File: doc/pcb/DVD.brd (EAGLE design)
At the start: 53.7 x 42.8 mm, 34 parts, among them IC1 7805, IC2 74HC14N

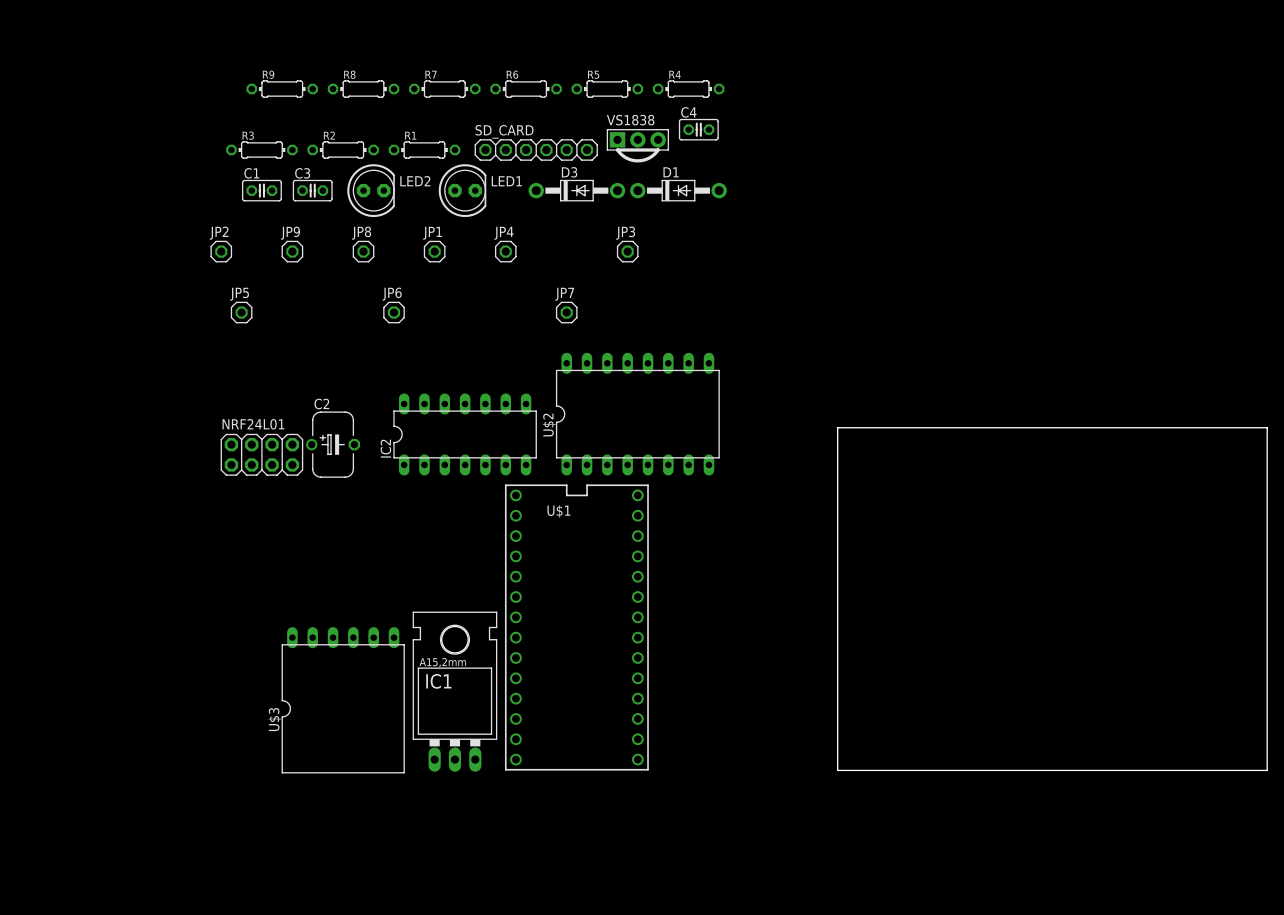
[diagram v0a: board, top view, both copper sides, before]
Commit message: PCB moved/added capacitors, changed voltage Pololu/BNO055, added pinouts & testpoints
Only 1 testpoint connected
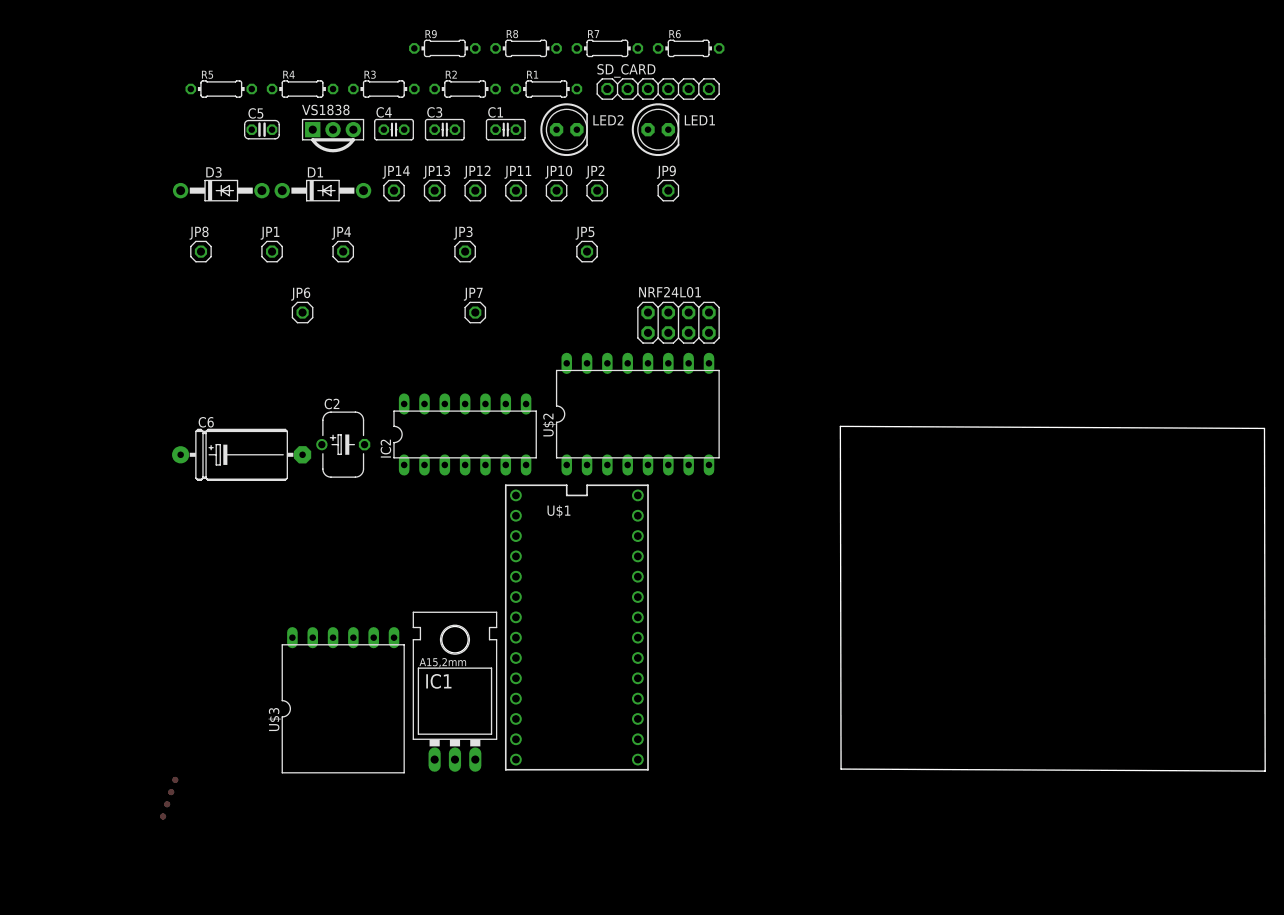
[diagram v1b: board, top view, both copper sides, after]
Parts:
- added C5: 100nF, rcl:C025-024X044
- added C6: 100uF, resistor:E15-6
- added JP10: P2, pinhead:1X01
- added JP11: P5, pinhead:1X01
- added JP12: P6, pinhead:1X01
- added JP13: P7, pinhead:1X01
- added JP14: P17, pinhead:1X01
- added TP1, TP2, TP3, TP4: TEST-POINT3, SparkFun-Passives:PAD.03X.03
- C1: value 0.1 uF -> 100 nF
- C2: value 1000 uF -> 0.22F
- R2, R4: value 3.3K -> 5.6K
- moved NRF24L01 54.6 mm to (-19.1, 57.1)
- moved R4 48.3 mm to (-66.0, 86.4)
- moved R5 48.3 mm to (-76.2, 86.4)
- moved JP2 47.6 mm to (-29.2, 73.7)
- moved JP9 47.6 mm to (-20.3, 73.7)
- moved D1 44.5 mm to (-63.5, 73.7)
- moved D3 44.5 mm to (-76.2, 73.7)
- moved JP5 43.8 mm to (-30.5, 66.0)
- moved VS1838 38.1 mm to (-62.2, 81.3)
- moved C4 38.1 mm to (-54.6, 81.3)
- moved C1 31.4 mm to (-40.6, 81.3)
- moved LED1 25.3 mm to (-21.6, 81.3)
- moved LED2 25.3 mm to (-33.0, 81.3)
- moved R6 20.9 mm to (-17.8, 91.4)
- moved R8 20.9 mm to (-38.1, 91.4)
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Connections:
- removed net N$8: LED2.A, R9.1
- new net N$4: LED2.K, R9.2
- net +3V3: no longer U$2.2, U$3.1
- net +5V: now also C1.1, C5.1, LED2.A, TP1.P$1, U$2.2, U$3.1; no longer SD_CARD.5
- net GND: now also C5.2, C6.-; no longer LED2.K
- net N$19: now also R9.1; no longer R9.2
- net N$20: now also JP10.1
- net N$21: now also JP12.1
- net N$22: now also JP13.1
- net N$3: now also JP11.1
- net N$6: now also JP14.1
- net V+: now also C6.+; no longer C1.1
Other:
- board size 53.7 x 42.8 mm -> 53.1 x 43.1 mm

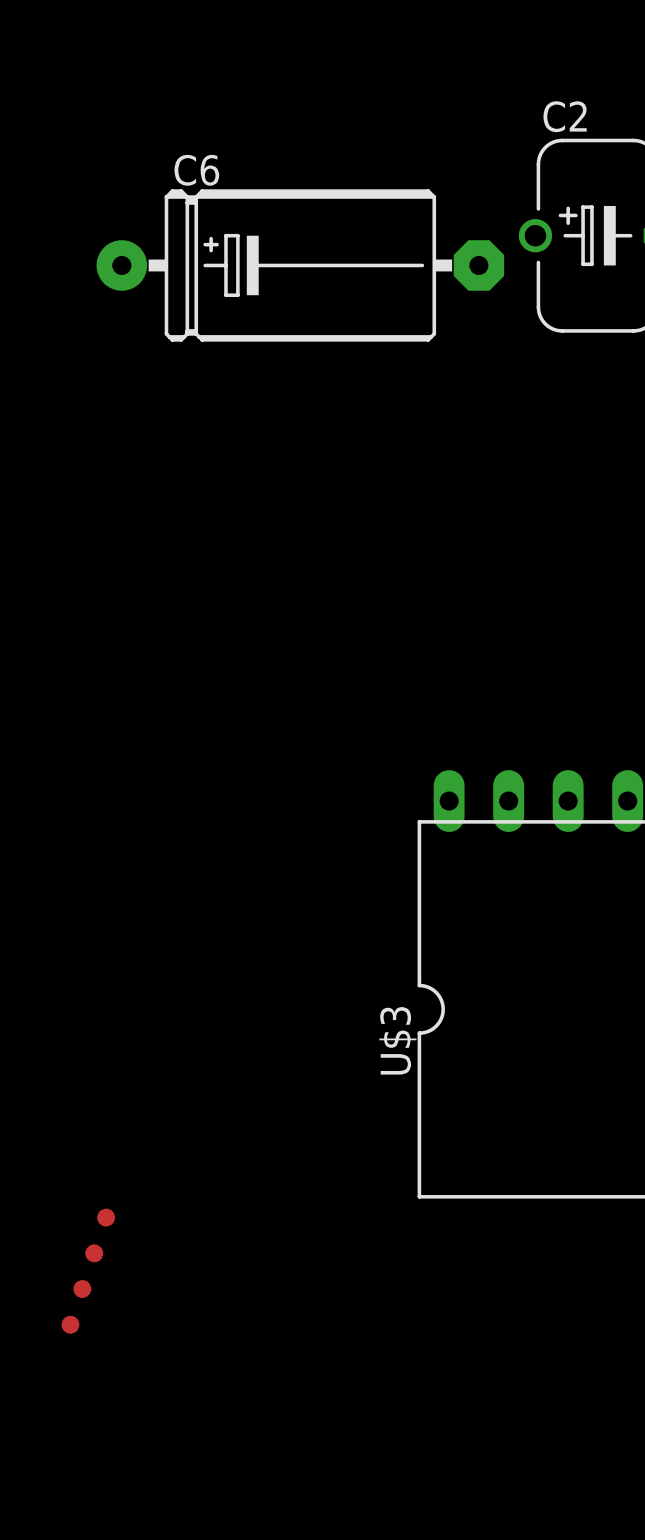
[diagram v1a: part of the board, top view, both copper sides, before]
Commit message: Replaced axial by radial capacitor
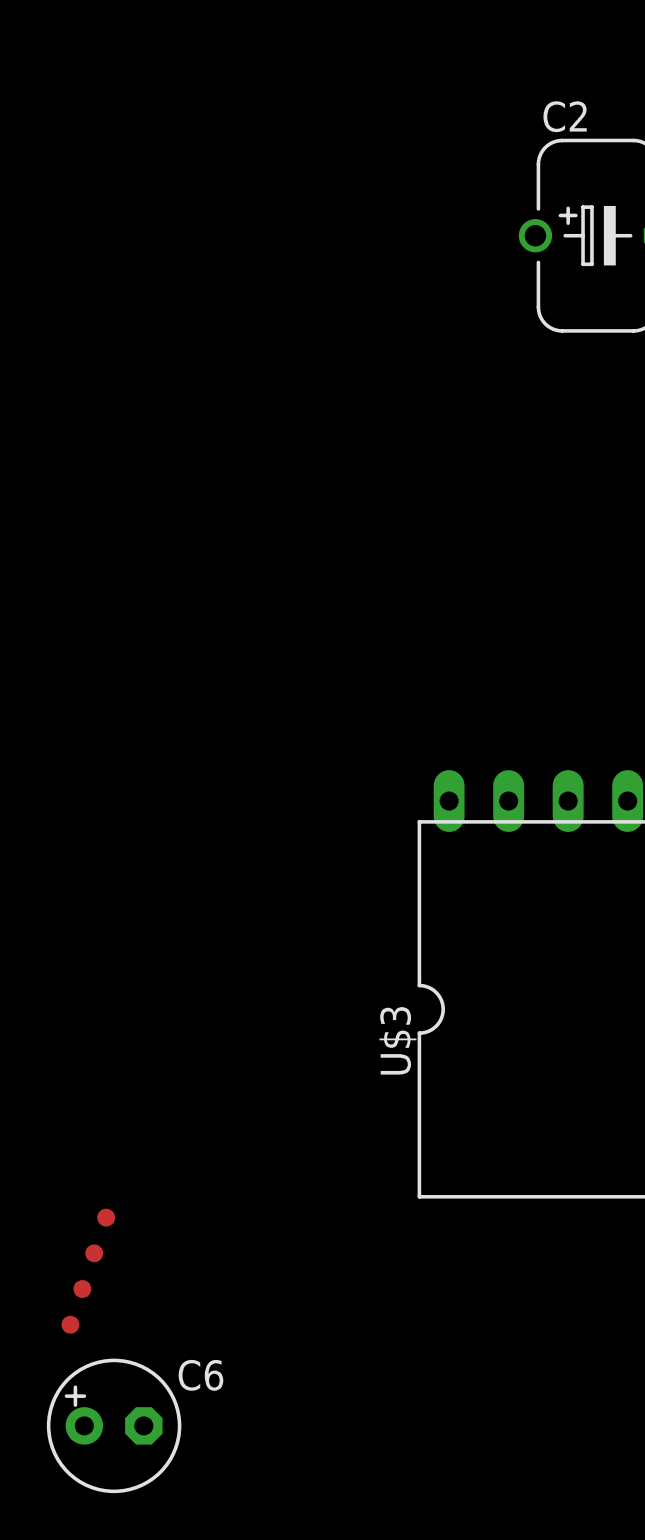
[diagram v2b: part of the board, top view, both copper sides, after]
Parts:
- C6: device resistor:E15-6 -> rcl:E2,5-6
- moved C6 50.2 mm to (-81.6, -8.89)
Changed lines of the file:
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@@
 <element name="C4" library="resistor" package="C025-025X050" value="100nF" x="-54.61" y="81.28"/>
 <element name="C5" library="rcl" package="C025-024X044" value="100nF" x="-71.12" y="81.28"/>
-<element name="C6" library="resistor" package="E15-6" value="100uF" x="-73.66" y="40.64"/>
 <element name="D1" library="adafruit" package="DO41-10" value="1N4004" x="-63.5" y="73.66"/>
 <element name="D3" library="adafruit" package="DO41-10" value="1N4004" x="-76.2" y="73.66"/>
@@
 <element name="TP3" library="SparkFun-Passives" package="PAD.03X.03" value="TEST-POINT3" x="-82.9650375" y="-3.04769375"/>
 <element name="TP4" library="SparkFun-Passives" package="PAD.03X.03" value="TEST-POINT3" x="-83.472984375" y="-4.57154375"/>
+<element name="C6" library="rcl" package="E2,5-6" value="100uF" x="-81.61050625" y="-8.8891125"/>
 </elements>
 <signals>
@@
 <contactref element="IC1" pad="IN"/>
 <contactref element="C6" pad="+"/>
+<wire x1="-49.53" y1="2.54" x2="-82.88050625" y2="-8.8891125" width="0" layer="19" extent="1-1"/>
+<wire x1="-17.78" y1="39.37" x2="-49.53" y2="2.54" width="0" layer="19" extent="1-1"/>
+<wire x1="-41.91" y1="86.36" x2="-17.78" y2="39.37" width="0" layer="19" extent="1-1"/>
 <wire x1="-68.58" y1="73.66" x2="-41.91" y2="86.36" width="0" layer="19" extent="1-1"/>
-<wire x1="-81.28" y1="40.64" x2="-68.58" y2="73.66" width="0" layer="19" extent="1-1"/>
-<wire x1="-49.53" y1="2.54" x2="-81.28" y2="40.64" width="0" layer="19" extent="1-1"/>
-<wire x1="-17.78" y1="39.37" x2="-49.53" y2="2.54" width="0" layer="19" extent="1-1"/>
 </signal>
 <signal name="GND">
@@
 <contactref element="C1" pad="2"/>
 <contactref element="C2" pad="-"/>
-<contactref element="C6" pad="-"/>
 <contactref element="U$1" pad="GND"/>
 <contactref element="VS1838" pad="2"/>
@@
 <contactref element="U$2" pad="1"/>
 <contactref element="U$2" pad="8"/>
-<wire x1="-20.32" y1="81.28" x2="-15.24" y2="86.36" width="0" layer="19" extent="1-1"/>
-<wire x1="-29.21" y1="73.66" x2="-20.32" y2="81.28" width="0" layer="19" extent="1-1"/>
+<contactref element="C6" pad="-"/>
+<wire x1="-62.23" y1="17.78" x2="-80.34050625" y2="-8.8891125" width="0" layer="19" extent="1-1"/>
+<wire x1="-46.99" y1="2.54" x2="-62.23" y2="17.78" width="0" layer="19" extent="1-1"/>
+<wire x1="-58.293" y1="41.91" x2="-62.23" y2="17.78" width="0" layer="19" extent="1-1"/>
+<wire x1="-39.37" y1="35.56" x2="-58.293" y2="41.91" width="0" layer="19" extent="1-1"/>
+<wire x1="-38.1" y1="39.37" x2="-39.37" y2="35.56" width="0" layer="19" extent="1-1"/>
+<wire x1="-33.02" y1="39.37" x2="-38.1" y2="39.37" width="0" layer="19" extent="1-1"/>
+<wire x1="-15.24" y1="39.37" x2="-33.02" y2="39.37" width="0" layer="19" extent="1-1"/>
+<wire x1="-15.24" y1="52.07" x2="-15.24" y2="39.37" width="0" layer="19" extent="1-1"/>
+<wire x1="-22.86" y1="55.88" x2="-15.24" y2="52.07" width="0" layer="19" extent="1-1"/>
+<wire x1="-29.21" y1="73.66" x2="-22.86" y2="55.88" width="0" layer="19" extent="1-1"/>
+<wire x1="-20.32" y1="81.28" x2="-29.21" y2="73.66" width="0" layer="19" extent="1-1"/>
+<wire x1="-15.24" y1="86.36" x2="-20.32" y2="81.28" width="0" layer="19" extent="1-1"/>
 <wire x1="-39.37" y1="81.28" x2="-29.21" y2="73.66" width="0" layer="19" extent="1-1"/>
 <wire x1="-46.99" y1="81.28" x2="-39.37" y2="81.28" width="0" layer="19" extent="1-1"/>
@@
 <wire x1="-45.72" y1="66.04" x2="-46.99" y2="81.28" width="0" layer="19" extent="1-1"/>
 <wire x1="-44.45" y1="58.42" x2="-45.72" y2="66.04" width="0" layer="19" extent="1-1"/>
-<wire x1="-22.86" y1="55.88" x2="-29.21" y2="73.66" width="0" layer="19" extent="1-1"/>
-<wire x1="-15.24" y1="52.07" x2="-22.86" y2="55.88" width="0" layer="19" extent="1-1"/>
-<wire x1="-15.24" y1="39.37" x2="-15.24" y2="52.07" width="0" layer="19" extent="1-1"/>
-<wire x1="-33.02" y1="39.37" x2="-15.24" y2="39.37" width="0" layer="19" extent="1-1"/>
-<wire x1="-38.1" y1="39.37" x2="-33.02" y2="39.37" width="0" layer="19" extent="1-1"/>
-<wire x1="-39.37" y1="35.56" x2="-38.1" y2="39.37" width="0" layer="19" extent="1-1"/>
-<wire x1="-58.293" y1="41.91" x2="-39.37" y2="35.56" width="0" layer="19" extent="1-1"/>
-<wire x1="-66.04" y1="40.64" x2="-58.293" y2="41.91" width="0" layer="19" extent="1-1"/>
-<wire x1="-62.23" y1="17.78" x2="-66.04" y2="40.64" width="0" layer="19" extent="1-1"/>
-<wire x1="-46.99" y1="2.54" x2="-62.23" y2="17.78" width="0" layer="19" extent="1-1"/>
 </signal>
 <signal name="+5V">

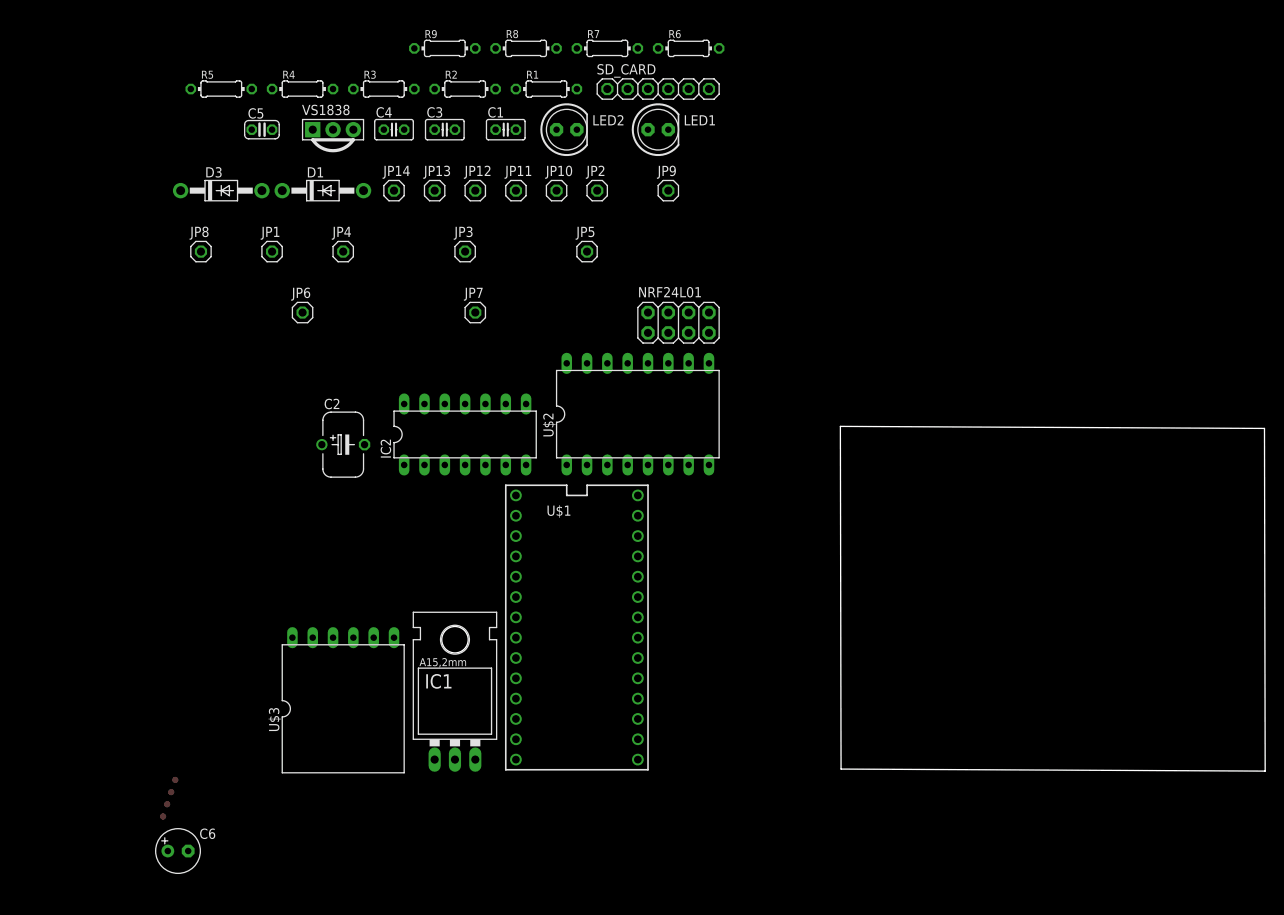
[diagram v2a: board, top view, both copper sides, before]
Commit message: Redid capacitor change
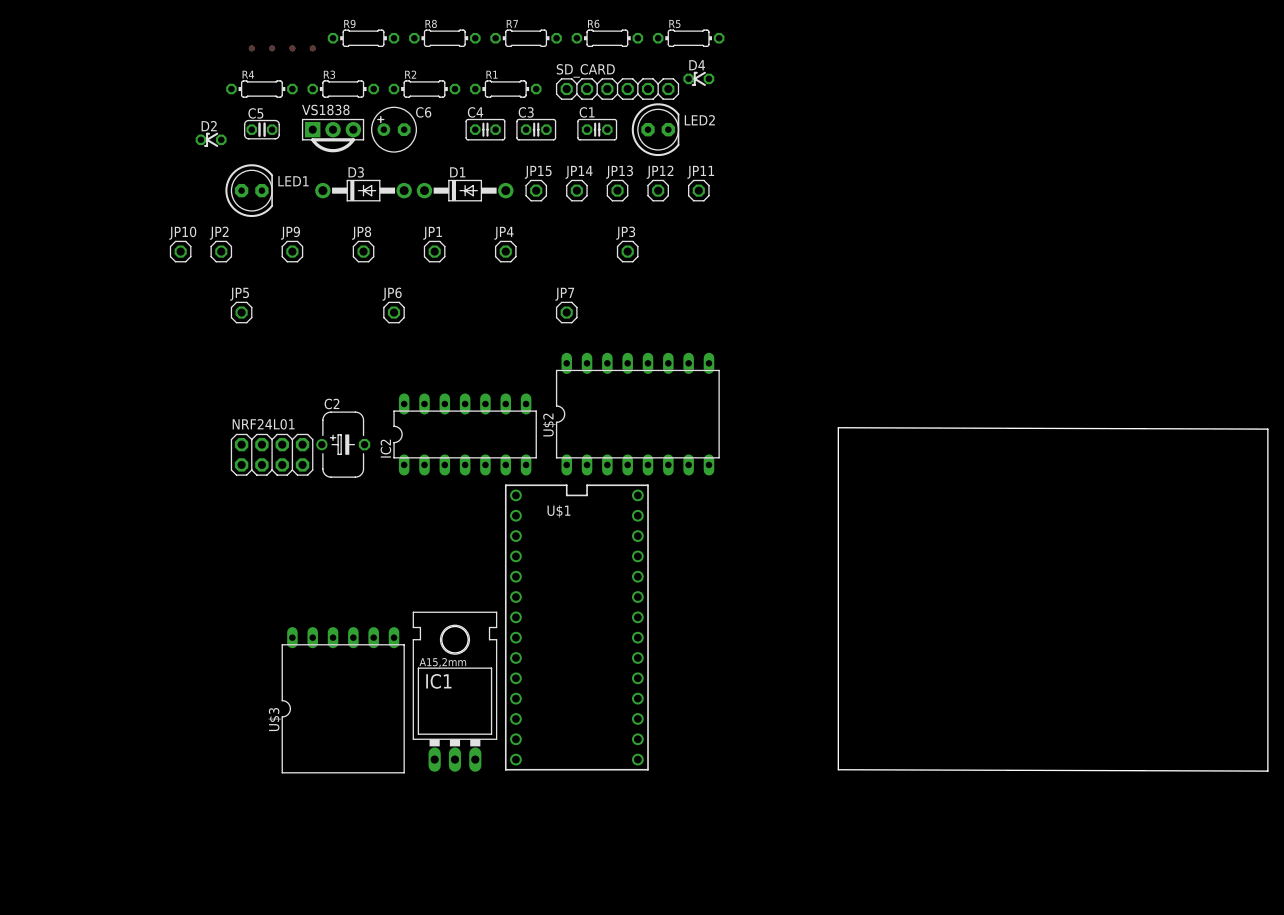
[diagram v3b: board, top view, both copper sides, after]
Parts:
- added D2, D4: ZF3.3, diode:ZDIO-2.5
- added JP15: GND, pinhead:1X01
- C6: value 100uF -> 100 uF
- D3: value 1N4004 -> 1N4148
- TP1: value TEST-POINT3 -> TEST-POINT1
- TP2: value TEST-POINT3 -> TEST-POINT2
- TP4: value TEST-POINT3 -> TEST-POINT4
- moved TP4 96.6 mm to (-72.4, 91.4)
- moved TP3 95.4 mm to (-69.8, 91.4)
- moved TP2 94.2 mm to (-67.3, 91.4)
- moved C6 94.1 mm to (-54.6, 81.3)
- moved TP1 93.0 mm to (-64.8, 91.4)
- moved R5 58.8 mm to (-17.8, 92.7)
- moved NRF24L01 53.4 mm to (-69.8, 40.6)
- moved LED1 51.4 mm to (-72.4, 73.7)
- moved JP10 47.6 mm to (-81.3, 66.0)
- moved JP2 47.6 mm to (-76.2, 66.0)
- moved JP9 47.6 mm to (-67.3, 66.0)
- moved JP5 43.8 mm to (-73.7, 58.4)
- moved JP12 22.9 mm to (-21.6, 73.7)
- moved JP13 22.9 mm to (-26.7, 73.7)
- moved JP14 22.9 mm to (-31.8, 73.7)
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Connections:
- net +3V3: now also TP2.P$1
- net GND: now also D2.A, D4.A
- net N$1: now also TP4.P$1
- net N$10: now also D4.C
- net N$11: now also D2.C
- net V+: now also TP3.P$1
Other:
- board size 53.1 x 43.1 mm -> 53.7 x 42.9 mm
